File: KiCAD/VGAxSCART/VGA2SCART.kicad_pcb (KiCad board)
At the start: 2 copper layers, 41.2 x 14.2 mm, 7 parts, among them P1 VGA, P2 SCART_PAL

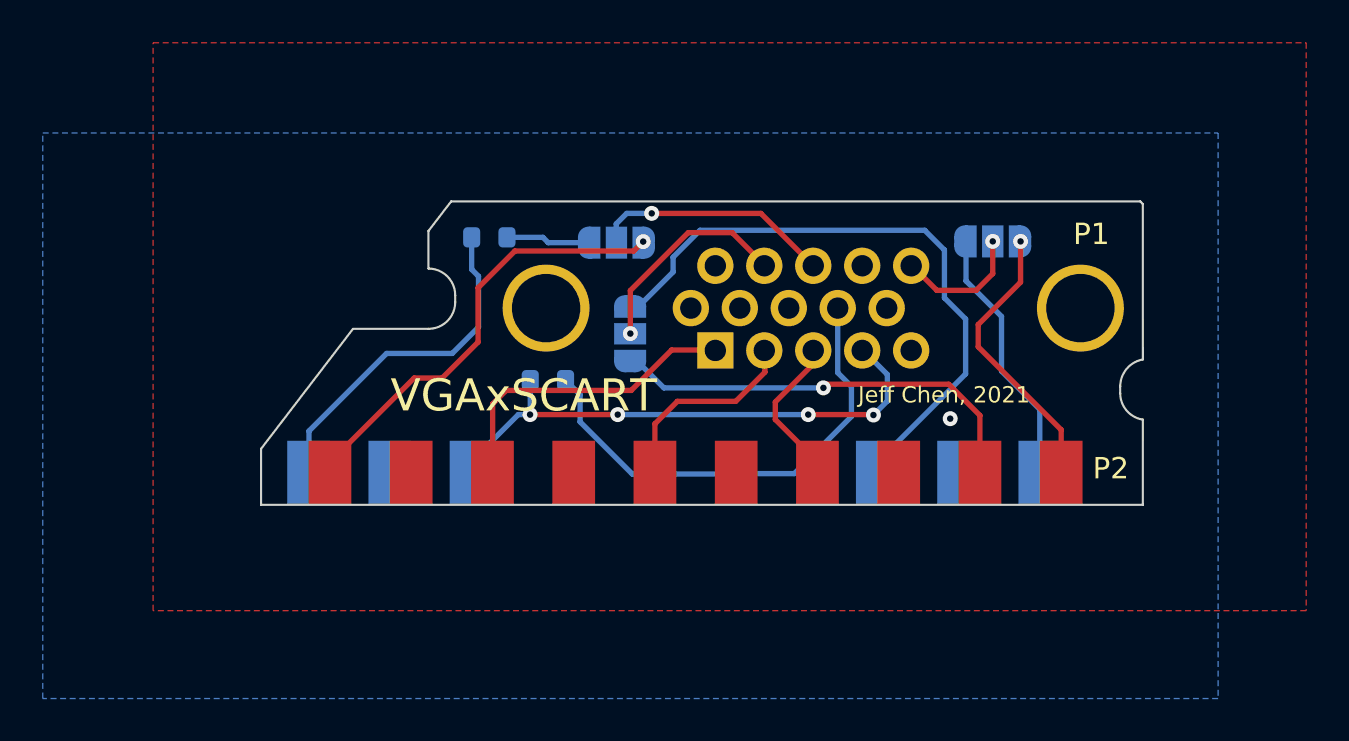
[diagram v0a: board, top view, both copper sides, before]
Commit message: Add Jumper for Non-CSync
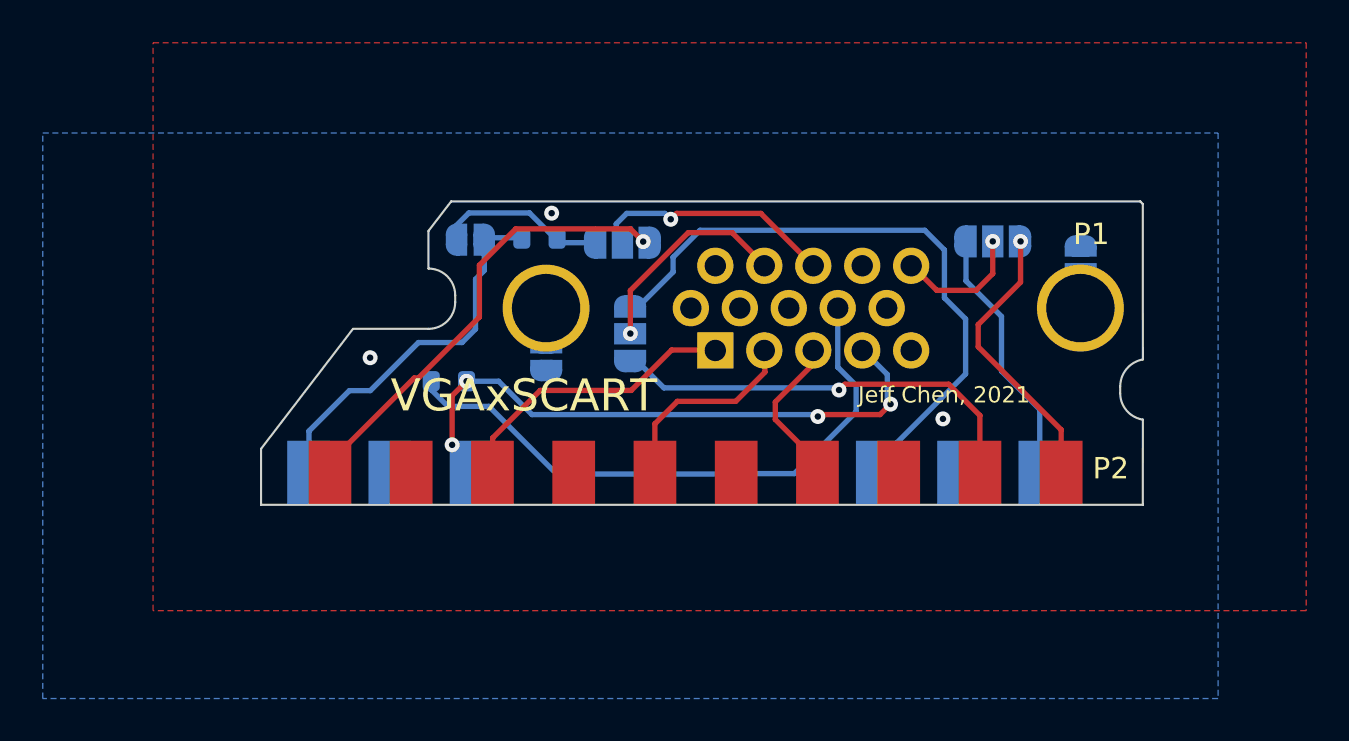
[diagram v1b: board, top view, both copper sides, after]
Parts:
- added JP4: SolderJumper_2_Open, Jumper:SolderJumper-2_P1.3mm_Open_RoundedPad1.0x1.5mm, B.Cu at (158.7, 93.1)
- added JP5: SolderJumper_2_Open, Jumper:SolderJumper-2_P1.3mm_Open_RoundedPad1.0x1.5mm, B.Cu at (133.7, 97.6)
- added JP6: No Attenuation, Jumper:SolderJumper-2_P1.3mm_Open_RoundedPad1.0x1.5mm, B.Cu at (130.1, 92.1)
- moved R1 4.63 mm to (129.1, 98.8), turned to 0 degrees
- moved R2 2.35 mm to (133.4, 92.1)
- moved JP1 0.28 mm to (137.2, 92.3)
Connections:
- P1 pad 11: (no net) -> unconnected-(P1-Pad11)
- P1 pad 14: (no net) -> unconnected-(P1-Pad14)
- P1 pad S1: GND -> Net-(JP4-Pad1)
- P1 pad S2: GND -> Net-(JP5-Pad1)
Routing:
- net Net-(P1-Pad9): track 22.5 -> 28.4 mm
- net /Attenuated_Sync: track 3.92 -> 7.67 mm
- net /Blanking: track 25.1 -> 27.1 mm
- net /CVBS_In: track 17.0 -> 18.5 mm
- net /Red: track 14.7 -> 13.8 mm
- net GND: vias 1 -> 3
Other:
- net class Default removed
- board text added: "Triangle: VGA to SCART NO Triangle: SCART to VGA"
- board text removed: "Triangle End: VGA to SCART The Other: SCART to VGA"
